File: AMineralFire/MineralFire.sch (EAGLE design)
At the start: 56 parts, among them IC1 LM358, Q1 20MHz, T1 200mA/40V, U1 328P, U3 7805

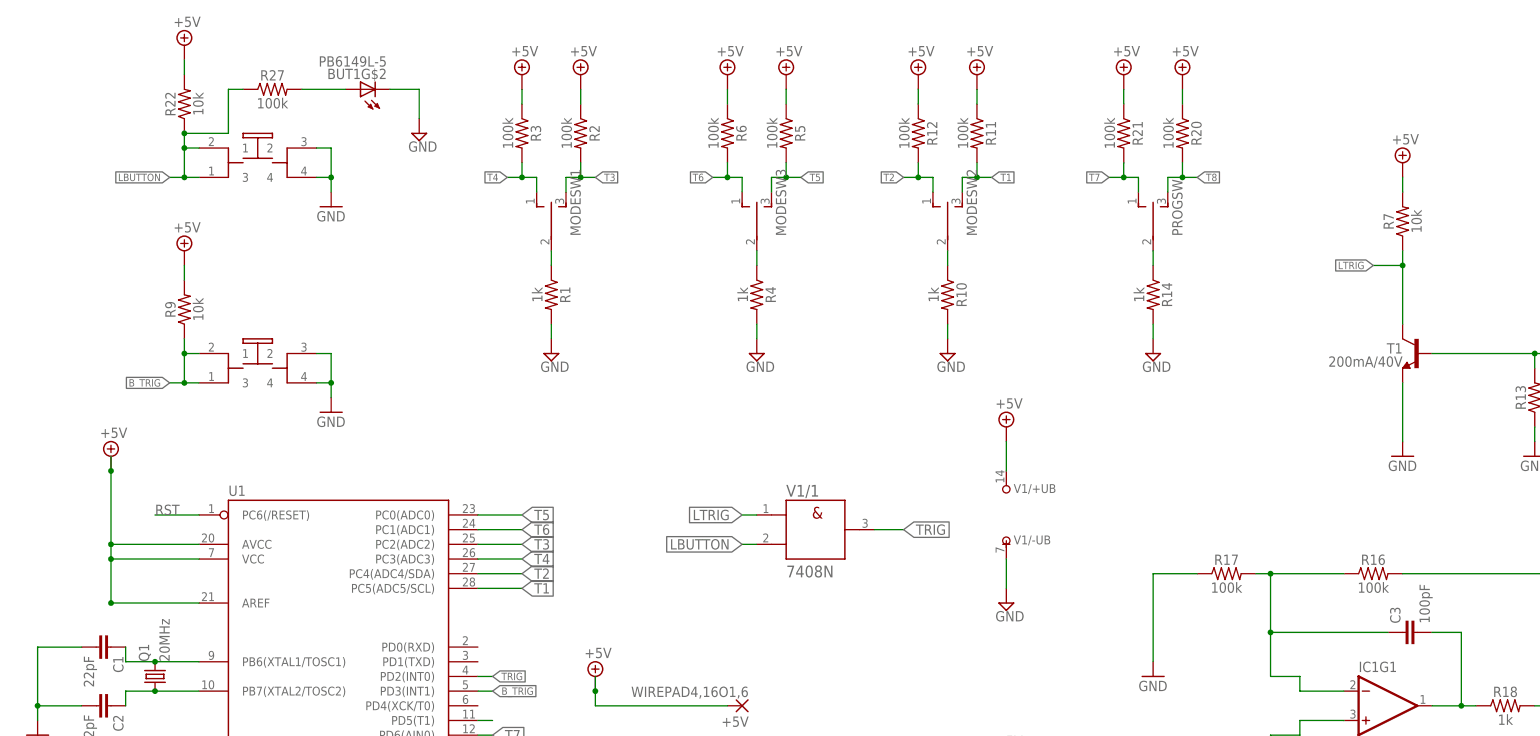
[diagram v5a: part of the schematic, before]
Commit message: LED in count switch
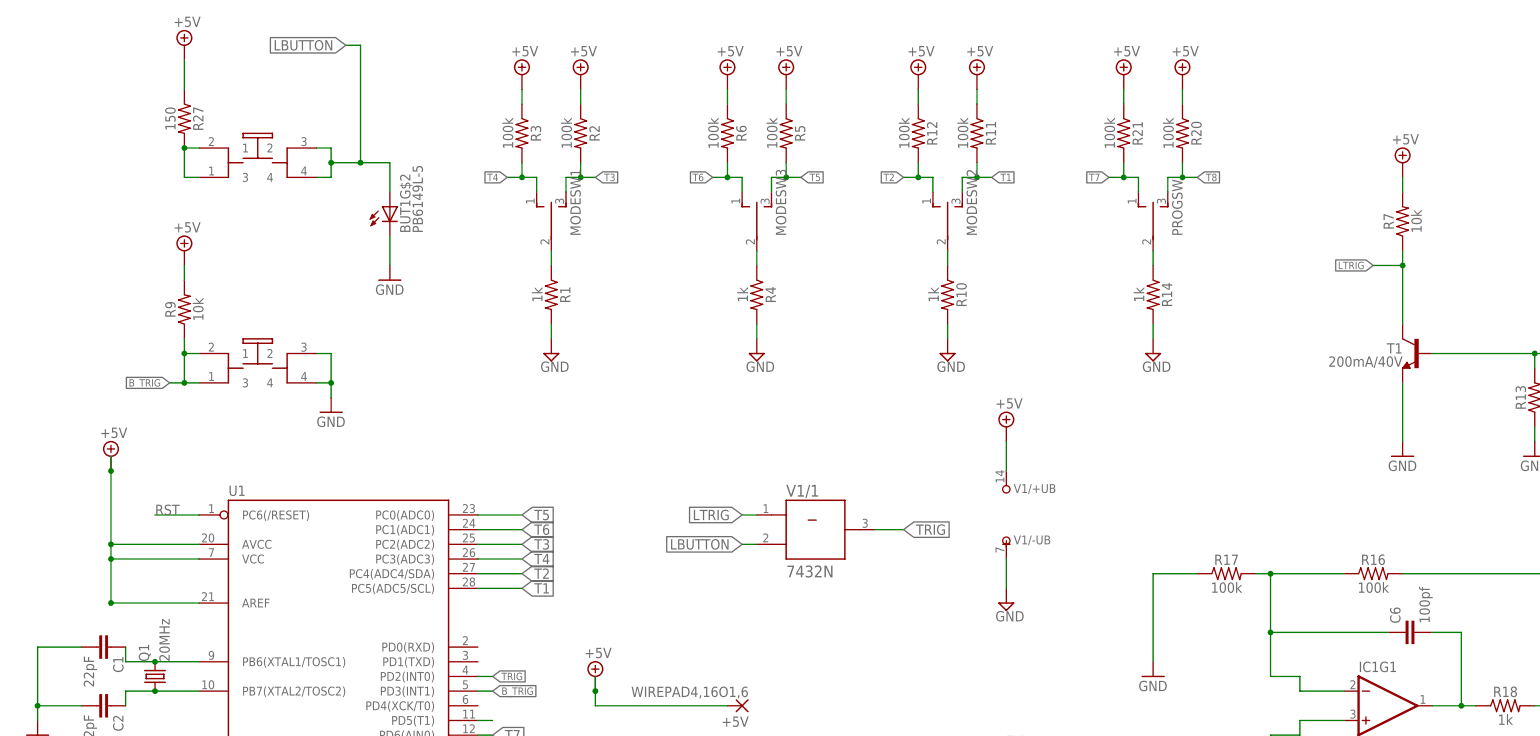
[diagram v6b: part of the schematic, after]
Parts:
- removed C3: 100pF, SparkFun-Capacitors:100PF-0603-50V-5%
- removed R22: 10k, SparkFun-Resistors:10KOHM-HORIZ-1/4W-1%
- added C6: 100pf, rcl:C-EU075-032X103
- R27: value 100k -> 150
- V1: value 7408N -> 7432N; device 74ttl-din:7408N -> 74ttl-din:7432N
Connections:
- removed net N$16: BUT1G$2.A, R27.2
- new net N$11: BUT1G$1.2, BUT1G$1.4, BUT1G$2.A
- net +5V: now also R27.1; no longer R22.2
- net GND: no longer BUT1G$1.2, BUT1G$1.4
- net LBUTTON: now also R27.2; no longer R22.1, R27.1
- net N$32: now also C6.1; no longer C3.1
- net N$33: now also C6.2; no longer C3.2
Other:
- moved on the sheet: BUT1G$2, R27
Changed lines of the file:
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@@
 <part name="R16" library="SparkFun-Resistors" deviceset="100KOHM" device="-HORIZ-1/4W-5%" value="100k"/>
 <part name="R17" library="SparkFun-Resistors" deviceset="100KOHM" device="-HORIZ-1/4W-5%" value="100k"/>
-<part name="C3" library="SparkFun-Capacitors" deviceset="100PF" device="-0603-50V-5%" value="100pF"/>
 <part name="R18" library="SparkFun-Resistors" deviceset="1KOHM" device="-HORIZ-1/4W-5%" value="1k"/>
 <part name="GND20" library="supply1" deviceset="GND" device=""/>
@@
 <part name="SUPPLY25" library="supply2" deviceset="+5V" device=""/>
 <part name="SUPPLY26" library="supply2" deviceset="+5V" device=""/>
-<part name="R22" library="SparkFun-Resistors" deviceset="10KOHM" device="-HORIZ-1/4W-1%" value="10k"/>
 <part name="SUPPLY27" library="supply2" deviceset="+5V" device=""/>
 <part name="GND5" library="supply1" deviceset="GND" device=""/>
 <part name="BUT" library="INSTRUO" deviceset="PB6149L-5" device="" value="PB6149L-5"/>
 <part name="BUT1" library="INSTRUO" deviceset="PB6149L-5" device="" value="PB6149L-5"/>
-<part name="R27" library="SparkFun-Resistors" deviceset="100KOHM" device="-HORIZ-1/4W-5%" value="100k"/>
-<part name="SUPPLY30" library="supply2" deviceset="GND" device=""/>
-<part name="V1" library="74ttl-din" deviceset="74*08" device="N"/>
+<part name="R27" library="SparkFun-Resistors" deviceset="100KOHM" device="-HORIZ-1/4W-5%" value="150"/>
+<part name="V1" library="74ttl-din" deviceset="74*32" device="N"/>
 <part name="SUPPLY28" library="supply2" deviceset="+5V" device=""/>
 <part name="SUPPLY29" library="supply2" deviceset="GND" device=""/>
+<part name="C6" library="rcl" deviceset="C-EU" device="075-032X103" value="100pf"/>
 </parts>
 <sheets>
@@
 <instance part="R16" gate="G$1" x="266.7" y="58.42"/>
 <instance part="R17" gate="G$1" x="241.3" y="58.42"/>
-<instance part="C3" gate="G$1" x="274.32" y="48.26" rot="R90"/>
 <instance part="R18" gate="G$1" x="289.56" y="35.56"/>
 <instance part="GND20" gate="1" x="228.6" y="40.64"/>
@@
 <instance part="SUPPLY25" gate="+5V" x="223.52" y="144.78"/>
 <instance part="SUPPLY26" gate="+5V" x="233.68" y="144.78"/>
-<instance part="R22" gate="G$1" x="60.96" y="139.7" rot="R90"/>
 <instance part="SUPPLY27" gate="+5V" x="60.96" y="149.86"/>
-<instance part="GND5" gate="1" x="86.36" y="121.92"/>
+<instance part="GND5" gate="1" x="96.52" y="109.22"/>
 <instance part="BUT" gate="G$1" x="73.66" y="96.52"/>
 <instance part="BUT" gate="G$2" x="256.54" y="17.78" rot="R90"/>
 <instance part="BUT1" gate="G$1" x="73.66" y="132.08"/>
-<instance part="BUT1" gate="G$2" x="91.44" y="142.24" rot="R90"/>
-<instance part="R27" gate="G$1" x="76.2" y="142.24"/>
-<instance part="SUPPLY30" gate="GND" x="101.6" y="134.62"/>
+<instance part="BUT1" gate="G$2" x="96.52" y="121.92"/>
+<instance part="R27" gate="G$1" x="60.96" y="137.16" rot="R270"/>
 <instance part="V1" gate="/1" x="170.18" y="66.04"/>
 <instance part="V1" gate="/+UB" x="203.2" y="73.66"/>
@@
 <instance part="V1" gate="/-UB" x="203.2" y="63.5"/>
 <instance part="SUPPLY29" gate="GND" x="203.2" y="53.34"/>
+<instance part="C6" gate="G$1" x="271.78" y="48.26" rot="R90"/>
 </instances>
 <busses>
@@
 </segment>
 <segment>
-<wire x1="83.82" y1="132.08" x2="86.36" y2="132.08" width="0.1524" layer="91"/>
-<wire x1="86.36" y1="132.08" x2="86.36" y2="127" width="0.1524" layer="91"/>
-<wire x1="86.36" y1="127" x2="86.36" y2="124.46" width="0.1524" layer="91"/>
-<wire x1="83.82" y1="127" x2="86.36" y2="127" width="0.1524" layer="91"/>
-<junction x="86.36" y="127"/>
-<pinref part="GND5" gate="1" pin="GND"/>
-<pinref part="BUT1" gate="G$1" pin="2"/>
-<pinref part="BUT1" gate="G$1" pin="4"/>
-</segment>
-<segment>
-<pinref part="BUT1" gate="G$2" pin="C"/>
-<wire x1="96.52" y1="142.24" x2="101.6" y2="142.24" width="0.1524" layer="91"/>
-<wire x1="101.6" y1="142.24" x2="101.6" y2="137.16" width="0.1524" layer="91"/>
-<pinref part="SUPPLY30" gate="GND" pin="GND"/>
-</segment>
-<segment>
 <pinref part="V1" gate="/-UB" pin="-UB"/>
 <wire x1="203.2" y1="60.96" x2="203.2" y2="55.88" width="0.1524" layer="91"/>
 <pinref part="SUPPLY29" gate="GND" pin="GND"/>
+</segment>
+<segment>
+<pinref part="BUT1" gate="G$2" pin="C"/>
+<wire x1="96.52" y1="116.84" x2="96.52" y2="111.76" width="0.1524" layer="91"/>
+<pinref part="GND5" gate="1" pin="GND"/>
 </segment>
 </net>
@@
 </segment>
 <segment>
-<pinref part="R22" gate="G$1" pin="2"/>
-<pinref part="SUPPLY27" gate="+5V" pin="+5V"/>
-<wire x1="60.96" y1="147.32" x2="60.96" y2="144.78" width="0.1524" layer="91"/>
-</segment>
-<segment>
 <pinref part="V1" gate="/+UB" pin="+UB"/>
 <wire x1="203.2" y1="76.2" x2="203.2" y2="81.28" width="0.1524" layer="91"/>
 <pinref part="SUPPLY28" gate="+5V" pin="+5V"/>
+</segment>
+<segment>
+<pinref part="SUPPLY27" gate="+5V" pin="+5V"/>
+<pinref part="R27" gate="G$1" pin="1"/>
+<wire x1="60.96" y1="147.32" x2="60.96" y2="142.24" width="0.1524" layer="91"/>
 </segment>
 </net>
@@
 <wire x1="248.92" y1="58.42" x2="261.62" y2="58.42" width="0.1524" layer="91"/>
 <junction x="248.92" y="58.42"/>
-<pinref part="C3" gate="G$1" pin="1"/>
 <wire x1="269.24" y1="48.26" x2="248.92" y2="48.26" width="0.1524" layer="91"/>
 <junction x="248.92" y="48.26"/>
@@
 <wire x1="261.62" y1="38.1" x2="254" y2="38.1" width="0.1524" layer="91"/>
 <wire x1="254" y1="38.1" x2="254" y2="40.64" width="0.1524" layer="91"/>
+<pinref part="C6" gate="G$1" pin="1"/>
 </segment>
 </net>
@@
 <wire x1="276.86" y1="35.56" x2="281.94" y2="35.56" width="0.1524" layer="91"/>
 <wire x1="281.94" y1="35.56" x2="281.94" y2="48.26" width="0.1524" layer="91"/>
-<pinref part="C3" gate="G$1" pin="2"/>
 <wire x1="281.94" y1="48.26" x2="276.86" y2="48.26" width="0.1524" layer="91"/>
 <pinref part="R18" gate="G$1" pin="1"/>
@@
 <junction x="281.94" y="35.56"/>
 <pinref part="IC1" gate="G1" pin="OUT"/>
+<pinref part="C6" gate="G$1" pin="2"/>
 </segment>
 </net>
@@
 </segment>
 </net>
-<net name="N$16" class="0">
-<segment>
-<pinref part="R27" gate="G$1" pin="2"/>
-<pinref part="BUT1" gate="G$2" pin="A"/>
-<wire x1="81.28" y1="142.24" x2="88.9" y2="142.24" width="0.1524" layer="91"/>
-</segment>
-</net>
 <net name="LTRIG" class="0">
 <segment>
@@
 </segment>
 <segment>
-<pinref part="R22" gate="G$1" pin="1"/>
 <wire x1="63.5" y1="132.08" x2="60.96" y2="132.08" width="0.1524" layer="91"/>
-<wire x1="60.96" y1="132.08" x2="60.96" y2="134.62" width="0.1524" layer="91"/>
 <wire x1="63.5" y1="127" x2="60.96" y2="127" width="0.1524" layer="91"/>
 <wire x1="60.96" y1="127" x2="60.96" y2="132.08" width="0.1524" layer="91"/>
-<junction x="60.96" y="132.08"/>
-<wire x1="60.96" y1="127" x2="58.42" y2="127" width="0.1524" layer="91"/>
-<junction x="60.96" y="127"/>
-<label x="58.42" y="127" size="1.27" layer="95" rot="R180" xref="yes"/>
-<wire x1="60.96" y1="134.62" x2="68.58" y2="134.62" width="0.1524" layer="91"/>
-<wire x1="68.58" y1="134.62" x2="68.58" y2="142.24" width="0.1524" layer="91"/>
-<junction x="60.96" y="134.62"/>
-<pinref part="R27" gate="G$1" pin="1"/>
-<wire x1="68.58" y1="142.24" x2="71.12" y2="142.24" width="0.1524" layer="91"/>
 <pinref part="BUT1" gate="G$1" pin="1"/>
 <pinref part="BUT1" gate="G$1" pin="3"/>
-</segment>
-</net>
+<label x="88.9" y="149.86" size="1.778" layer="95" rot="R180" xref="yes"/>
+<pinref part="R27" gate="G$1" pin="2"/>
+<junction x="60.96" y="132.08"/>
+</segment>
+</net>
+<net name="N$11" class="1">
+<segment>
+<wire x1="83.82" y1="132.08" x2="86.36" y2="132.08" width="0.1524" layer="91"/>
+<wire x1="86.36" y1="132.08" x2="86.36" y2="129.54" width="0.1524" layer="91"/>
+<wire x1="86.36" y1="129.54" x2="86.36" y2="127" width="0.1524" layer="91"/>
+<wire x1="83.82" y1="127" x2="86.36" y2="127" width="0.1524" layer="91"/>
+<pinref part="BUT1" gate="G$1" pin="2"/>
+<pinref part="BUT1" gate="G$1" pin="4"/>
+<junction x="86.36" y="129.54"/>
+<wire x1="86.36" y1="129.54" x2="91.44" y2="129.54" width="0.1524" layer="91"/>
+<pinref part="BUT1" gate="G$2" pin="A"/>
+<wire x1="91.44" y1="129.54" x2="96.52" y2="129.54" width="0.1524" layer="91"/>
+<wire x1="96.52" y1="129.54" x2="96.52" y2="124.46" width="0.1524" layer="91"/>
+<wire x1="88.9" y1="149.86" x2="91.44" y2="149.86" width="0.1524" layer="91"/>
+<wire x1="91.44" y1="149.86" x2="91.44" y2="129.54" width="0.1524" layer="91"/>
+<junction x="91.44" y="129.54"/>
+</segment>
+</net>

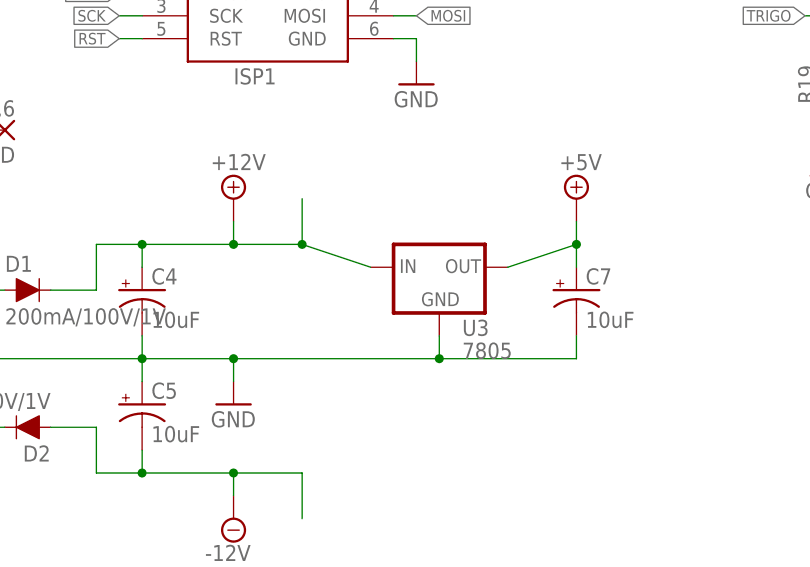
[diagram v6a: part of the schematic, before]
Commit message: Board too big
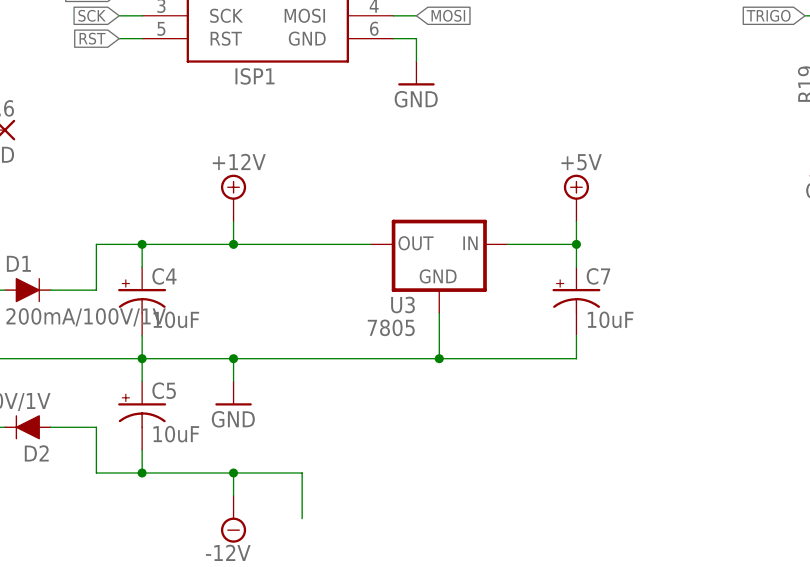
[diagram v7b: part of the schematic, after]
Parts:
- U3: device SparkFun-IC-Power:R-78E5.0-1.0 -> SparkFun-IC-Power:V_REG_78XX-TO-220
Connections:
- net +12V: now also U3.OUT; no longer U3.IN
- net +5V: now also U3.IN; no longer U3.OUT
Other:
- moved on the sheet: U3
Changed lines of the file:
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@@
 <part name="R11" library="SparkFun-Resistors" deviceset="100KOHM" device="-HORIZ-1/4W-5%" value="100k"/>
 <part name="R12" library="SparkFun-Resistors" deviceset="100KOHM" device="-HORIZ-1/4W-5%" value="100k"/>
-<part name="U3" library="SparkFun-IC-Power" deviceset="R-78E5.0-1.0" device="" value="7805"/>
+<part name="U3" library="SparkFun-IC-Power" deviceset="V_REG_78XX" device="-TO-220" value="7805"/>
 <part name="C7" library="SparkFun-Capacitors" deviceset="10UF-POLAR" device="-RADIAL-2.5MM-25V-20%" value="10uF"/>
 <part name="SUPPLY10" library="supply2" deviceset="+5V" device=""/>
@@
 <instance part="R11" gate="G$1" x="198.12" y="134.62" rot="R270"/>
 <instance part="R12" gate="G$1" x="187.96" y="134.62" rot="R270"/>
-<instance part="U3" gate="G$1" x="205.74" y="-10.16"/>
+<instance part="U3" gate="G$1" x="205.74" y="-7.62" rot="MR0"/>
 <instance part="C7" gate="G$1" x="220.98" y="-12.7"/>
 <instance part="SUPPLY10" gate="+5V" x="220.98" y="-2.54"/>
@@
 <pinref part="U3" gate="G$1" pin="GND"/>
 <wire x1="182.88" y1="-20.32" x2="205.74" y2="-20.32" width="0.1524" layer="91"/>
-<wire x1="205.74" y1="-20.32" x2="205.74" y2="-17.78" width="0.1524" layer="91"/>
+<wire x1="205.74" y1="-20.32" x2="205.74" y2="-15.24" width="0.1524" layer="91"/>
 <junction x="182.88" y="-20.32"/>
 <pinref part="C7" gate="G$1" pin="-"/>
@@
 </segment>
 <segment>
-<pinref part="U3" gate="G$1" pin="OUT"/>
 <pinref part="C7" gate="G$1" pin="+"/>
-<wire x1="213.36" y1="-10.16" x2="220.98" y2="-7.62" width="0.1524" layer="91"/>
-<wire x1="220.98" y1="-7.62" x2="220.98" y2="-10.16" width="0.1524" layer="91"/>
 <pinref part="SUPPLY10" gate="+5V" pin="+5V"/>
 <wire x1="220.98" y1="-5.08" x2="220.98" y2="-7.62" width="0.1524" layer="91"/>
+<pinref part="U3" gate="G$1" pin="IN"/>
+<wire x1="220.98" y1="-7.62" x2="220.98" y2="-10.16" width="0.1524" layer="91"/>
+<wire x1="213.36" y1="-7.62" x2="220.98" y2="-7.62" width="0.1524" layer="91"/>
 <junction x="220.98" y="-7.62"/>
 </segment>
@@
 <junction x="172.72" y="-7.62"/>
 <pinref part="SUPPLY4" gate="+12V" pin="+12V"/>
-<wire x1="182.88" y1="-7.62" x2="190.5" y2="-7.62" width="0.1524" layer="91"/>
+<pinref part="U3" gate="G$1" pin="OUT"/>
+<wire x1="182.88" y1="-7.62" x2="198.12" y2="-7.62" width="0.1524" layer="91"/>
 <junction x="182.88" y="-7.62"/>
-<wire x1="190.5" y1="-7.62" x2="190.5" y2="-2.54" width="0.1524" layer="91"/>
-<pinref part="U3" gate="G$1" pin="IN"/>
-<wire x1="190.5" y1="-7.62" x2="198.12" y2="-10.16" width="0.1524" layer="91"/>
-<junction x="190.5" y="-7.62"/>
-</segment>
-<segment>
+</segment>
+<segment>
